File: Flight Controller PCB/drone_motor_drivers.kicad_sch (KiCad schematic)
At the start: 0 parts

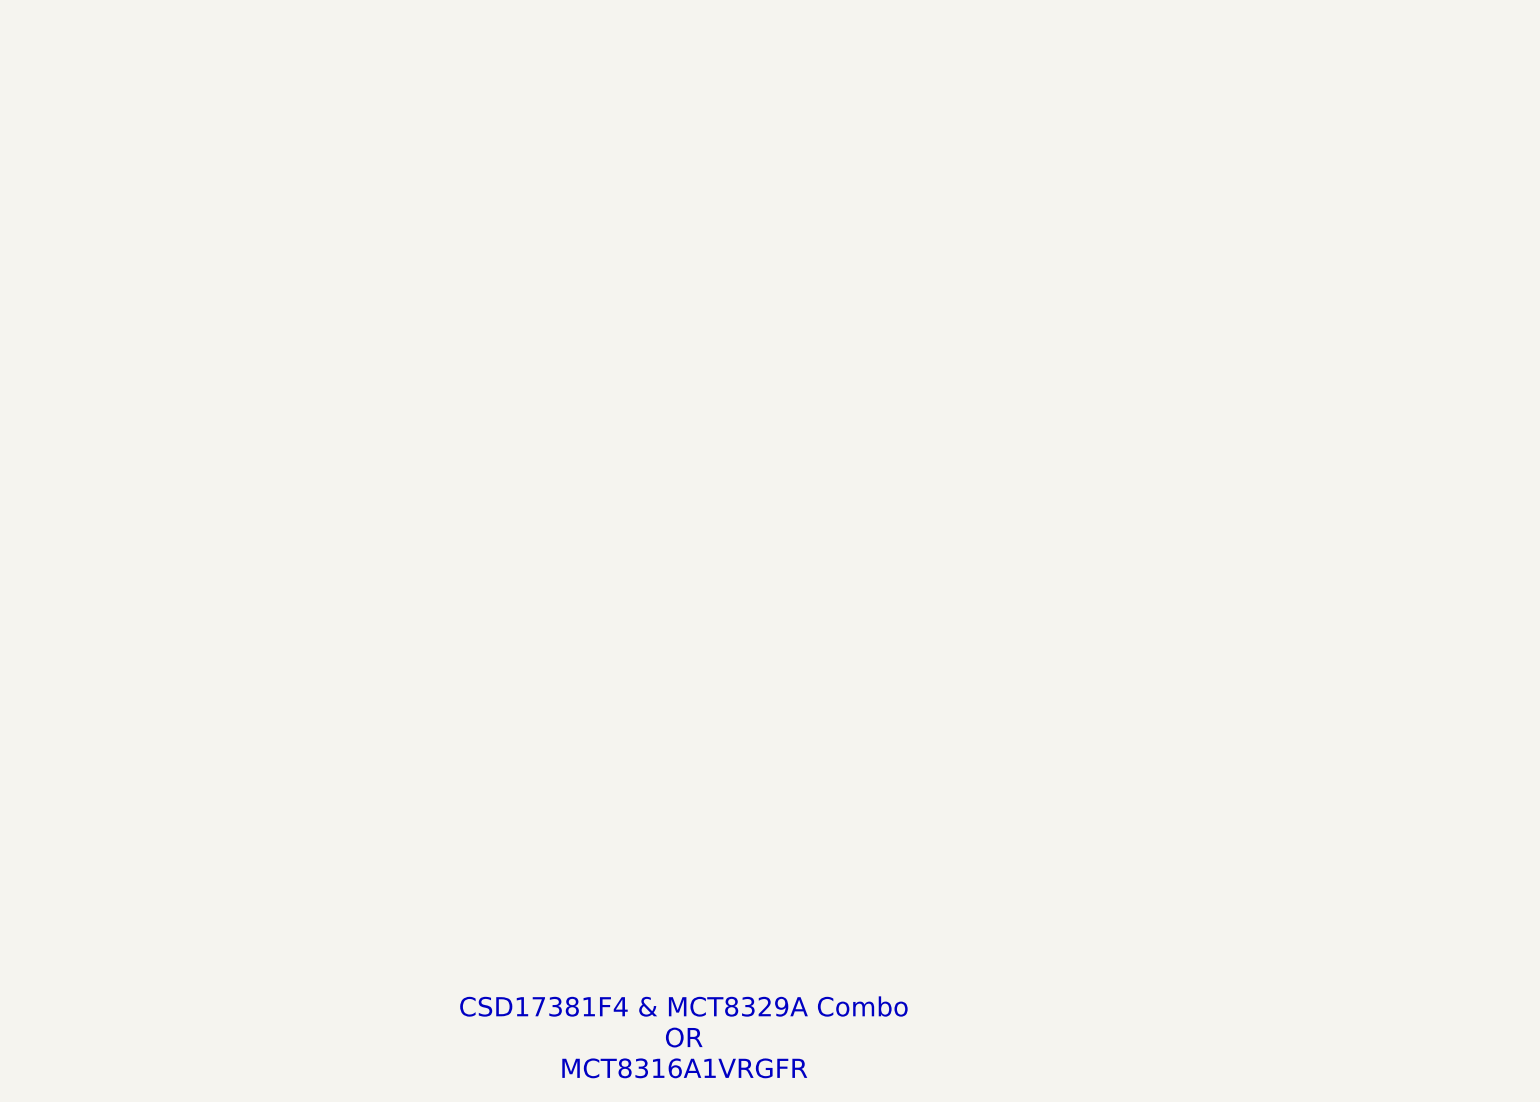
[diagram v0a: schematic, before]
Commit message: Selected motor controller, fixed MCU schematic and added I2C pullups
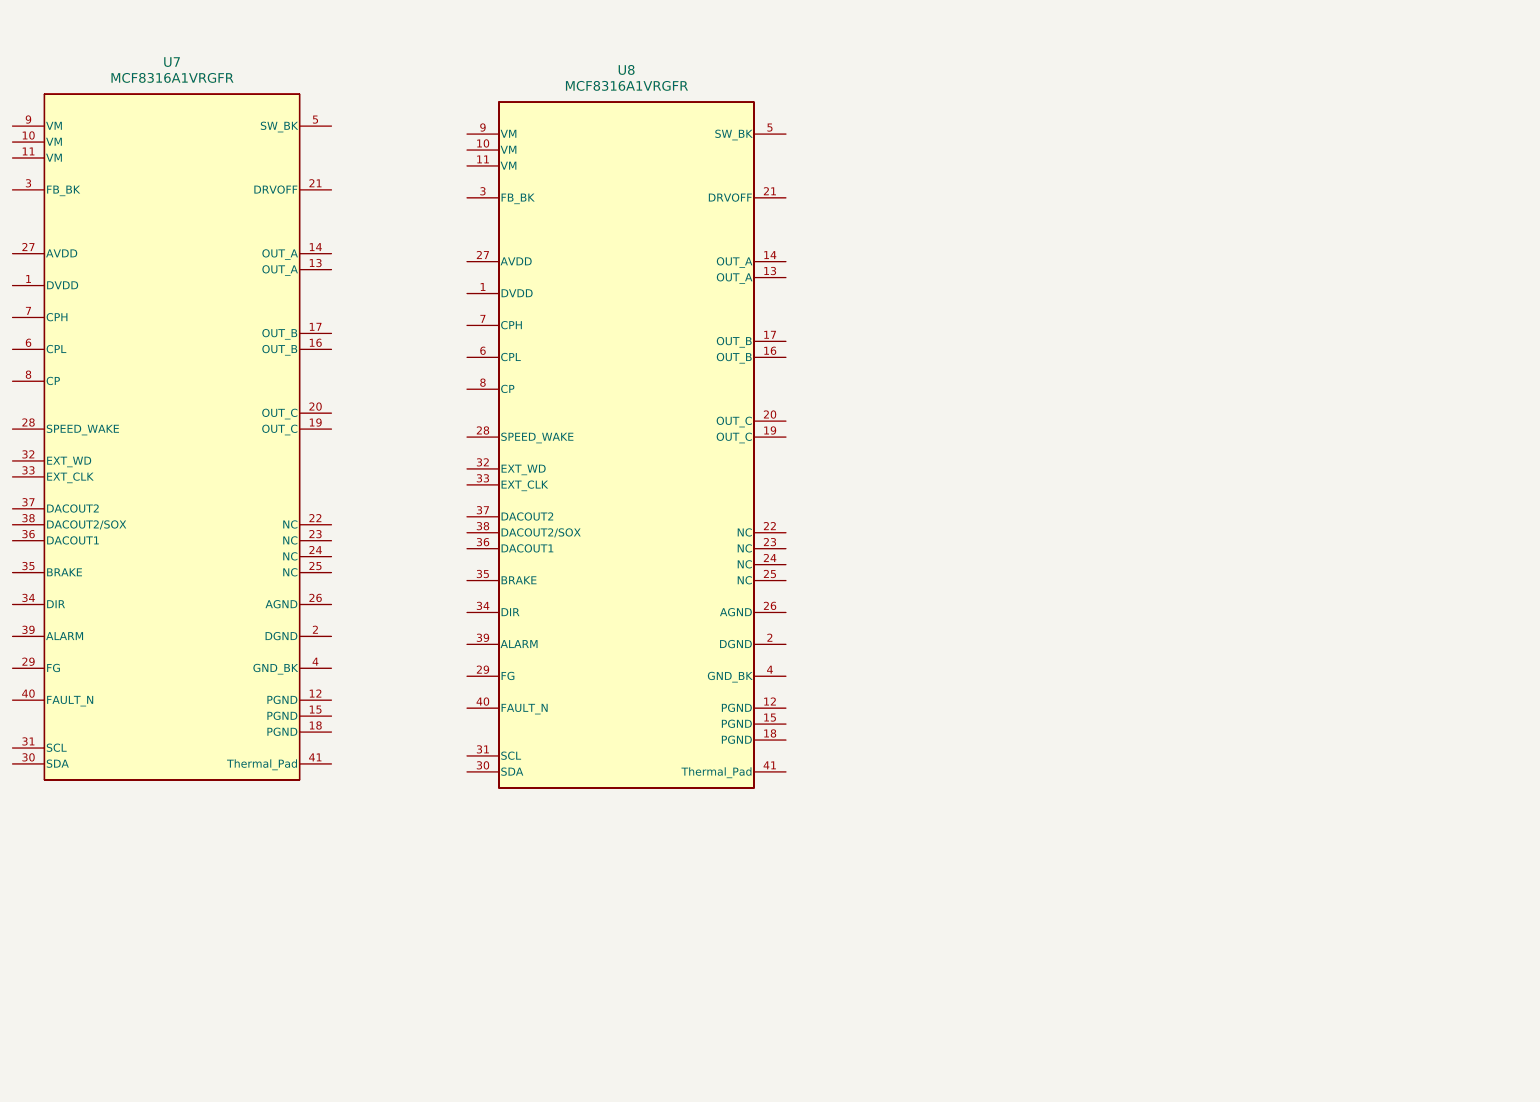
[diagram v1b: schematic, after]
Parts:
- added U7, U8: MCF8316A1VRGFR, RGF0040E-IPC_A, symbol Drone_sym:MCF8316A1VRGFR
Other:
- note removed: "CSD17381F4 & MCT8329A Combo OR MCT8316A1VRGFR"

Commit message: Some changes. TODO: Add power and control for RunCam2. Add battery voltage monitoring
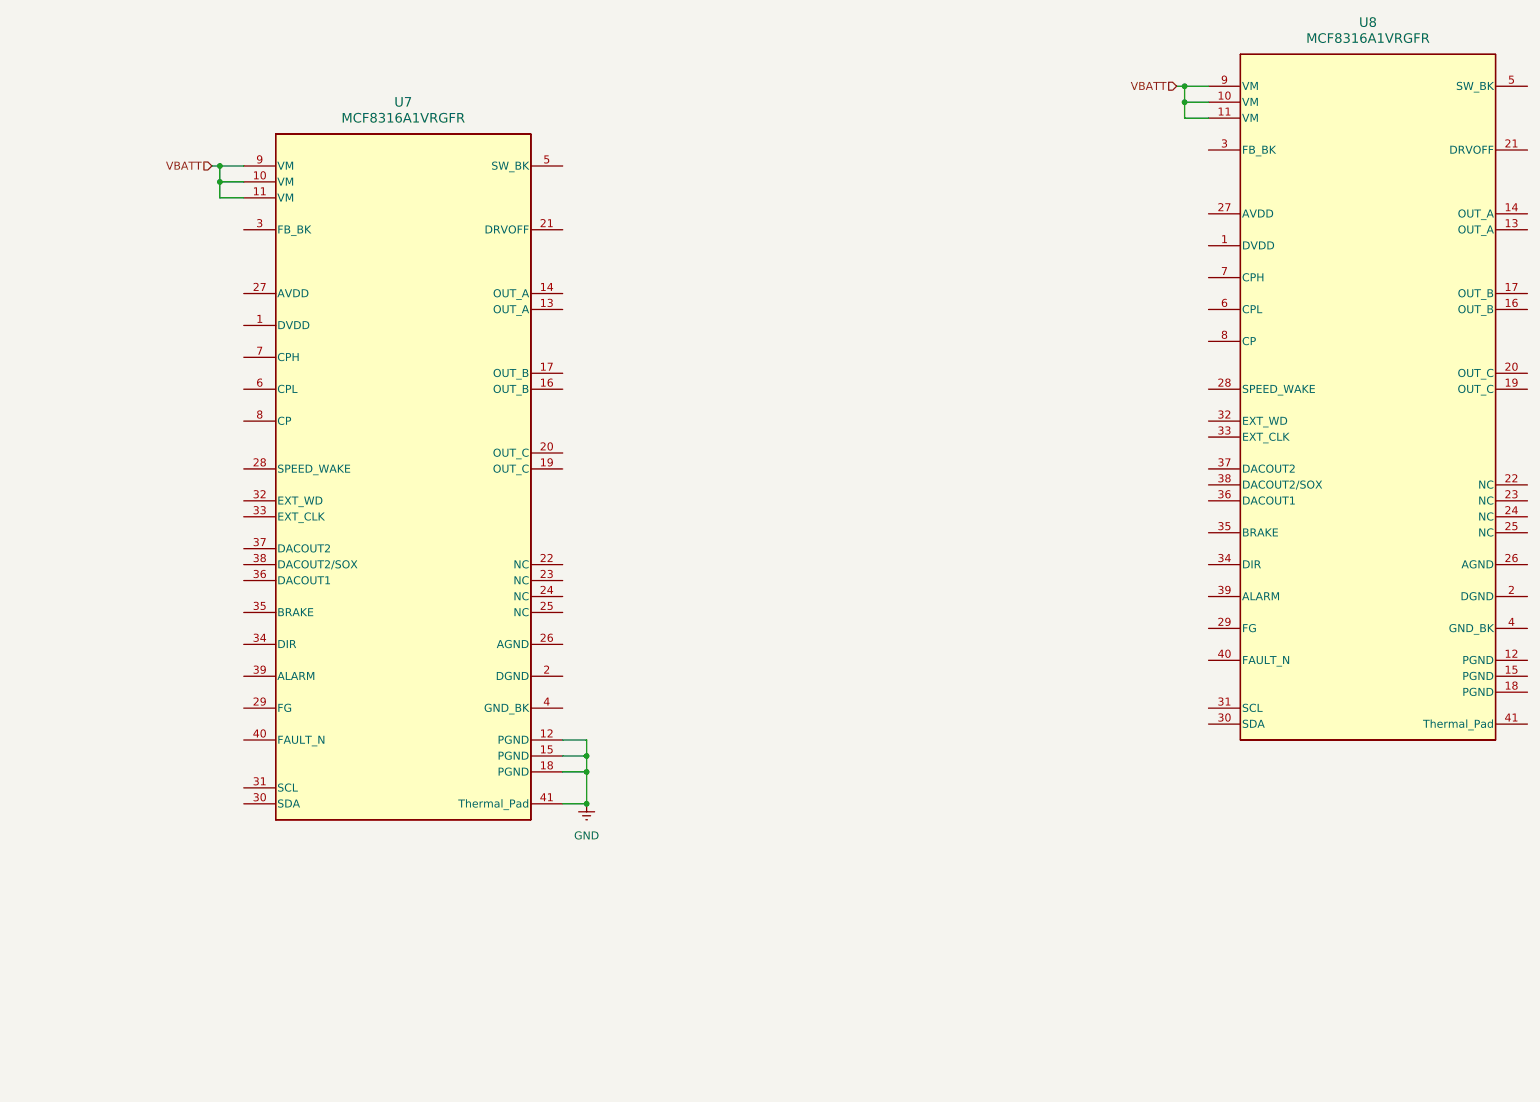
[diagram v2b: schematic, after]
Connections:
- net VBATT: now reaches U7.10 (VM)
- net VBATT: now also U7.11 (VM), U7.9 (VM), U8.10 (VM), U8.11 (VM), U8.9 (VM)
- net GND: now reaches U7.12 (PGND)
- net GND: now also U7.15 (PGND), U7.18 (PGND), U7.41 (Thermal_Pad)
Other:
- moved on the sheet: U7, U8

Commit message: Init
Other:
- moved on the sheet: U8
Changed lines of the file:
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@@
 	)
 	(junction
-		(at 213.36 22.86)
+		(at 156.21 36.83)
 		(diameter 0)
 		(color 0 0 0 0)
@@
 	)
 	(junction
-		(at 213.36 25.4)
+		(at 156.21 39.37)
 		(diameter 0)
 		(color 0 0 0 0)
@@
 	(wire
 		(pts
-			(xy 213.36 25.4) (xy 213.36 27.94)
-		)
-		(stroke
-			(width 0)
-			(type default)
-		)
-	)
-	(wire
-		(pts
-			(xy 212.09 22.86) (xy 213.36 22.86)
+			(xy 156.21 39.37) (xy 156.21 41.91)
+		)
+		(stroke
+			(width 0)
+			(type default)
+		)
+	)
+	(wire
+		(pts
+			(xy 154.94 36.83) (xy 156.21 36.83)
 		)
 		(stroke
@@
 	(wire
 		(pts
-			(xy 213.36 22.86) (xy 213.36 25.4)
+			(xy 156.21 36.83) (xy 156.21 39.37)
 		)
 		(stroke
@@
 	(wire
 		(pts
-			(xy 213.36 22.86) (xy 217.17 22.86)
+			(xy 156.21 36.83) (xy 160.02 36.83)
 		)
 		(stroke
@@
 	(wire
 		(pts
-			(xy 213.36 25.4) (xy 217.17 25.4)
-		)
-		(stroke
-			(width 0)
-			(type default)
-		)
-	)
-	(wire
-		(pts
-			(xy 213.36 27.94) (xy 217.17 27.94)
+			(xy 156.21 39.37) (xy 160.02 39.37)
+		)
+		(stroke
+			(width 0)
+			(type default)
+		)
+	)
+	(wire
+		(pts
+			(xy 156.21 41.91) (xy 160.02 41.91)
 		)
 		(stroke
@@
 	(hierarchical_label "VBATT"
 		(shape input)
-		(at 212.09 22.86 180)
+		(at 154.94 36.83 180)
 		(effects
 			(font
@@
 	(symbol
 		(lib_id "Drone_sym:MCF8316A1VRGFR")
-		(at 217.17 22.86 0)
+		(at 160.02 36.83 0)
 		(unit 1)
 		(body_style 1)
@@
 		(fields_autoplaced yes)
 		(property "Reference" "U8"
-			(at 242.57 12.7 0)
+			(at 185.42 26.67 0)
 			(show_name no)
 			(do_not_autoplace no)
@@
 		)
 		(property "Value" "MCF8316A1VRGFR"
-			(at 242.57 15.24 0)
+			(at 185.42 29.21 0)
 			(show_name no)
 			(do_not_autoplace no)
@@
 		)
 		(property "Footprint" "RGF0040E-IPC_A"
-			(at 217.17 22.86 0)
+			(at 160.02 36.83 0)
 			(hide yes)
 			(show_name no)
@@
 		)
 		(property "Datasheet" "https://www.ti.com/lit/gpn/mcf8316a"
-			(at 217.17 22.86 0)
+			(at 160.02 36.83 0)
 			(hide yes)
 			(show_name no)
@@
 		)
 		(property "Description" ""
-			(at 217.17 22.86 0)
-			(hide yes)
-			(show_name no)
+			(at 160.02 36.83 0)
+			(hide yes)
+			(show_name no)
